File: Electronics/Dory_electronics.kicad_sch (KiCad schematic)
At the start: 10 parts, among them J1 Bateria 2s, J2 Conn_01x08, J3 Conn_01x08, J4 |Motor 2, J5 Motor 1, J6 sensor IR, U1 LM7805_TO220

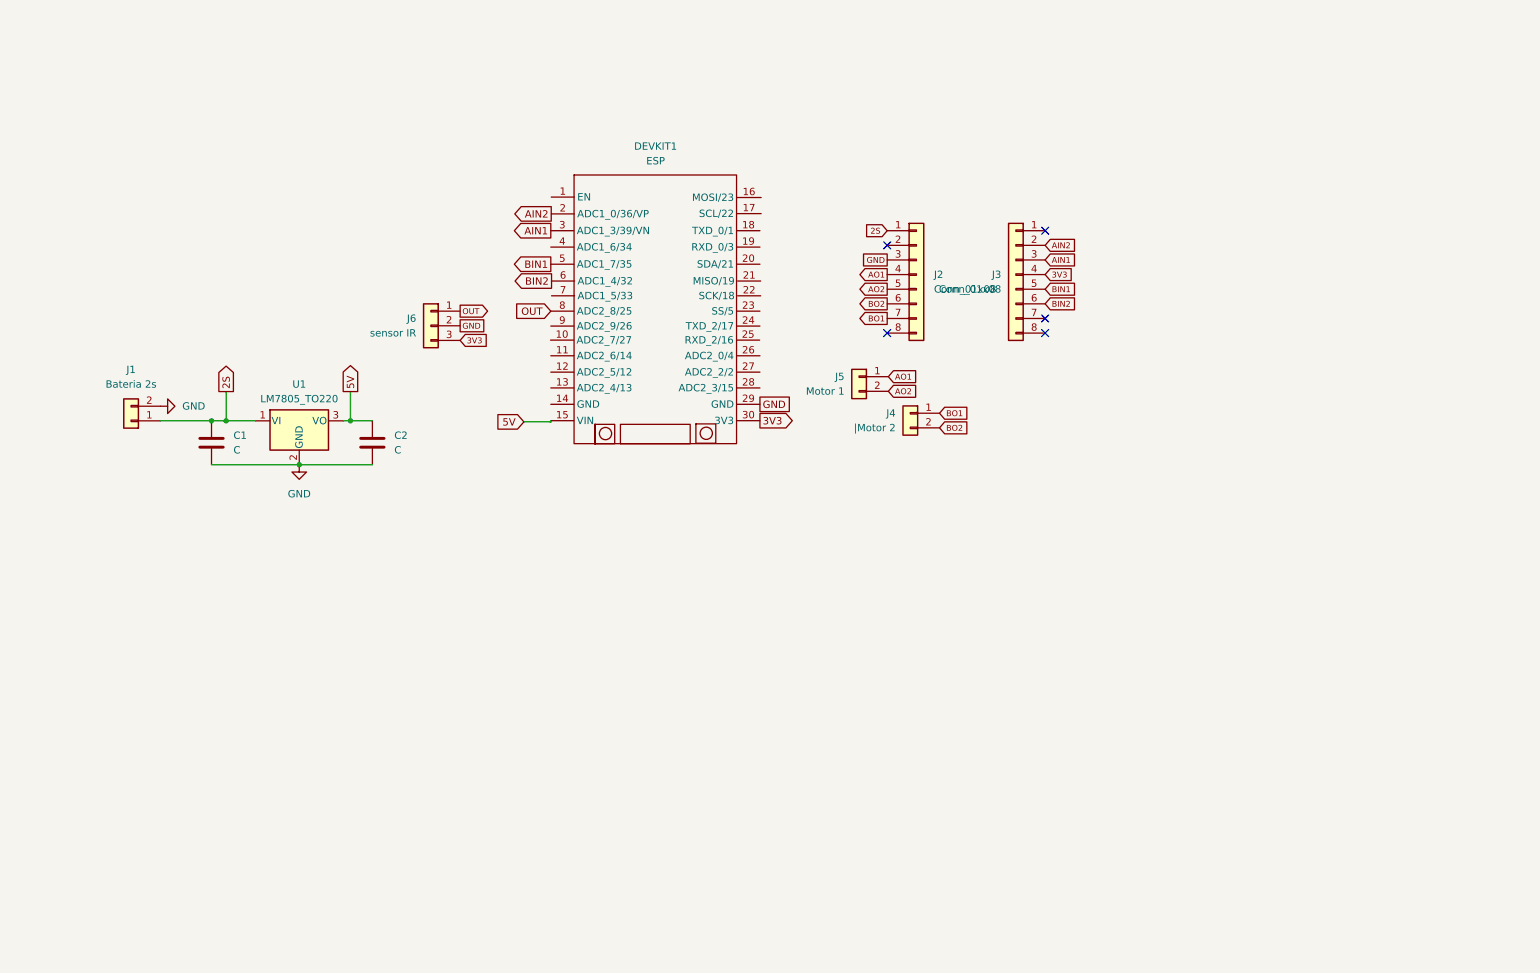
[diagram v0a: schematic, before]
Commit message: chore: organize schematic and add gitignore
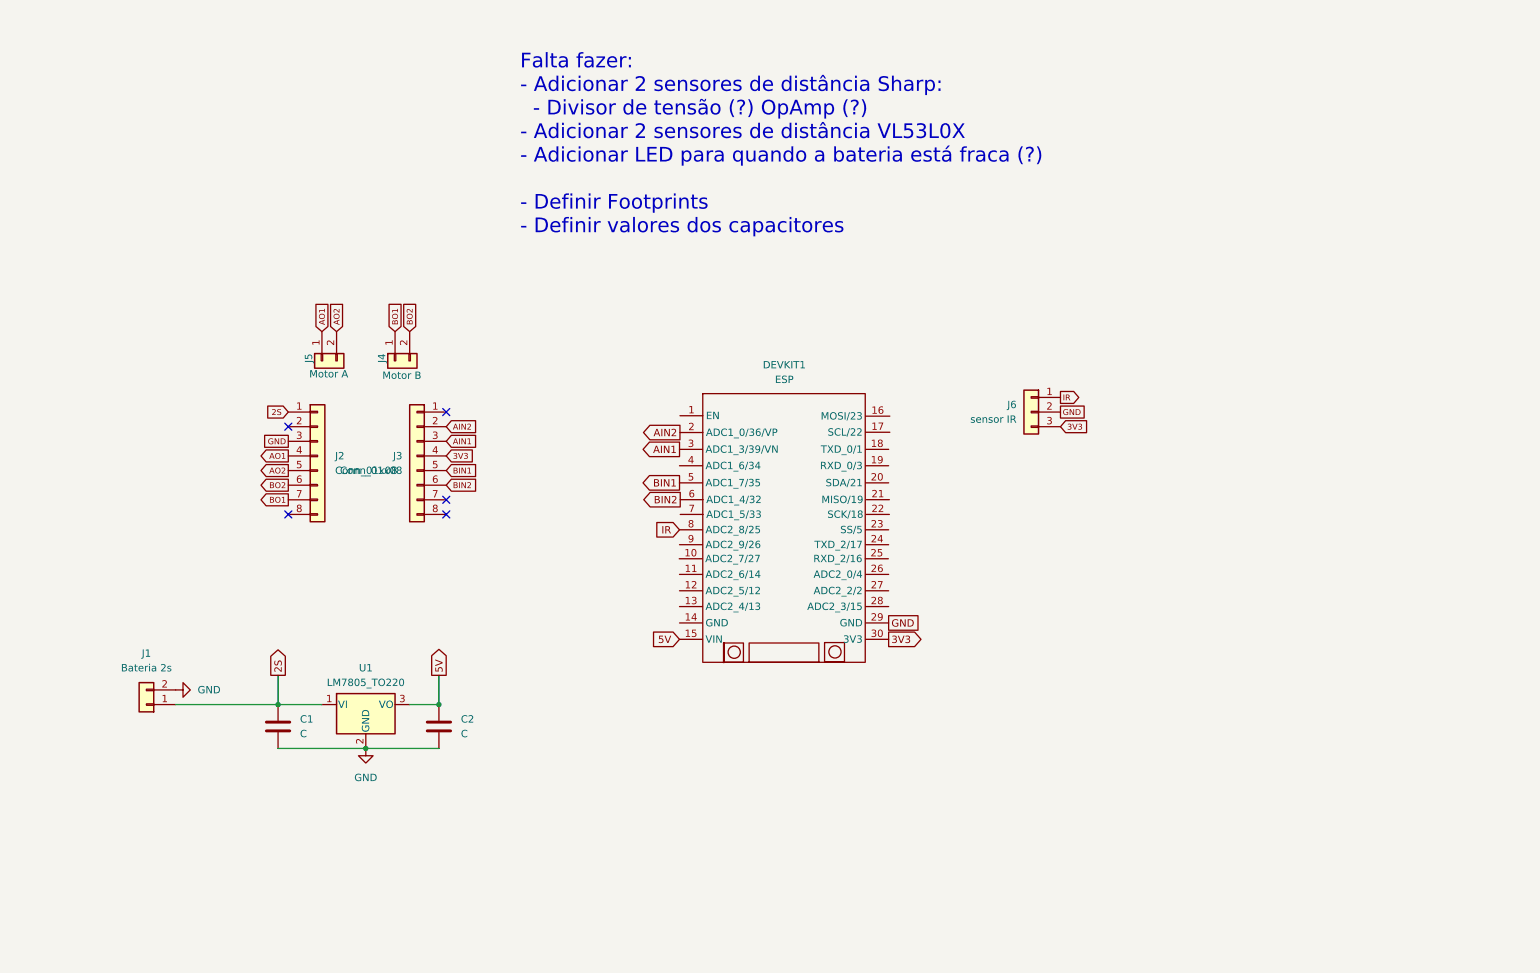
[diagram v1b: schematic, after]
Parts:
- J4: value |Motor 2 -> Motor B
- J5: value Motor 1 -> Motor A
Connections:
- net OUT renamed IR
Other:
- note added: "Falta fazer: - Adicionar 2 sensores de distância Sharp: - Divisor de tensão (?) OpAmp (?) - Adicionar 2 sensores de distância VL53L0X - Adicionar LED para quando a bateria está fraca (?) - Definir Footprints - Definir valores dos capacitores"
- moved on the sheet: C1, C2, DEVKIT1, J1, J2, J3, J4, J5, J6, U1

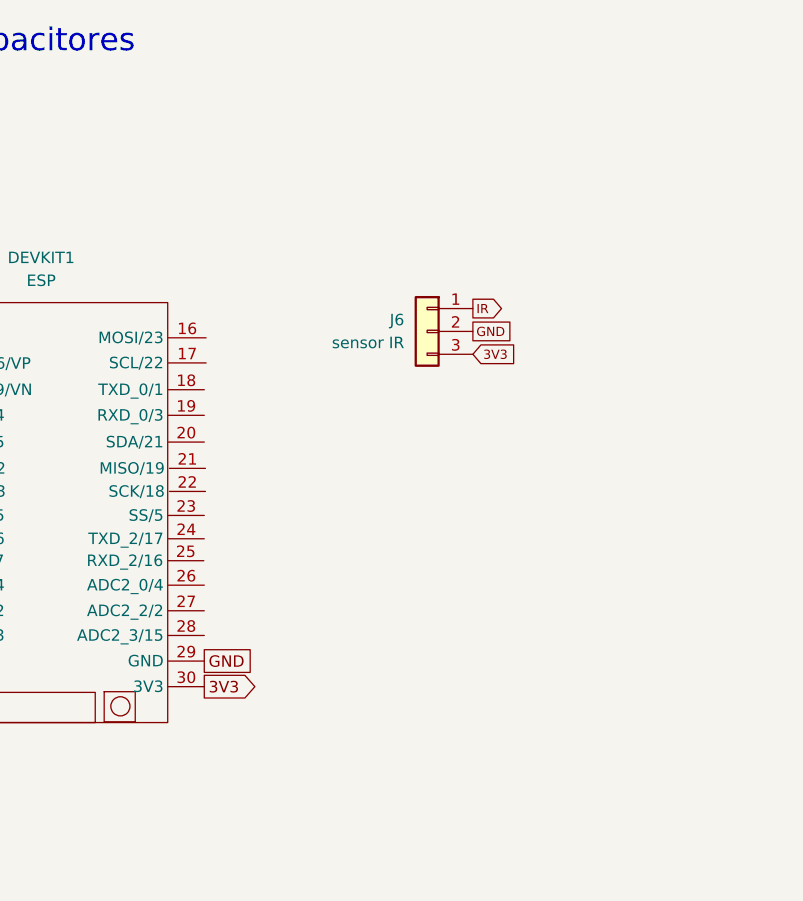
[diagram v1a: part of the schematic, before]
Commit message: feat: add VL530X
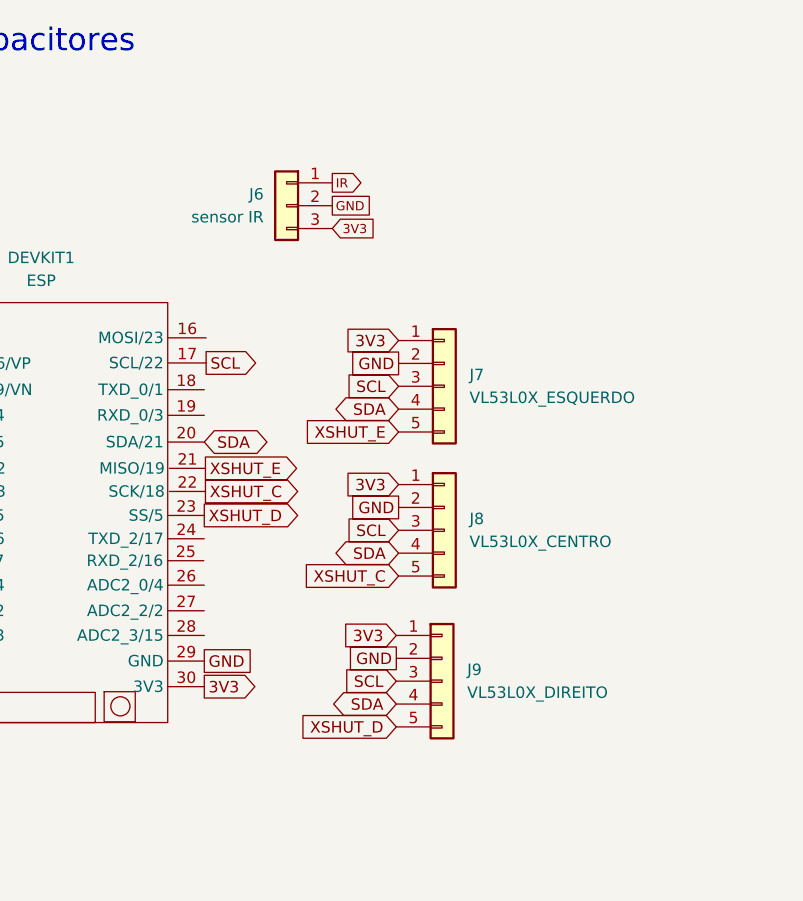
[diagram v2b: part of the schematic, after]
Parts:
- added J7: VL53L0X_ESQUERDO, symbol Connector_Generic:Conn_01x05
- added J8: VL53L0X_CENTRO, symbol Connector_Generic:Conn_01x05
- added J9: VL53L0X_DIREITO, symbol Connector_Generic:Conn_01x05
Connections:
- net 3V3: now also J7.1 (Pin_1), J8.1 (Pin_1), J9.1 (Pin_1)
- net GND: now also J7.2 (Pin_2), J8.2 (Pin_2), J9.2 (Pin_2)
- net SCL: now reaches DEVKIT1.17 (SCL/22)
- net SCL: now also J7.3 (Pin_3), J8.3 (Pin_3), J9.3 (Pin_3)
- net SDA: now reaches DEVKIT1.20 (SDA/21)
- net SDA: now also J7.4 (Pin_4), J8.4 (Pin_4), J9.4 (Pin_4)
- net XSHUT_E: now reaches DEVKIT1.21 (MISO/19)
- net XSHUT_E: now also J7.5 (Pin_5)
- net XSHUT_C: now reaches DEVKIT1.22 (SCK/18)
- net XSHUT_C: now also J8.5 (Pin_5)
- net XSHUT_D: now reaches DEVKIT1.23 (SS/5)
- net XSHUT_D: now also J9.5 (Pin_5)
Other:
- moved on the sheet: J6

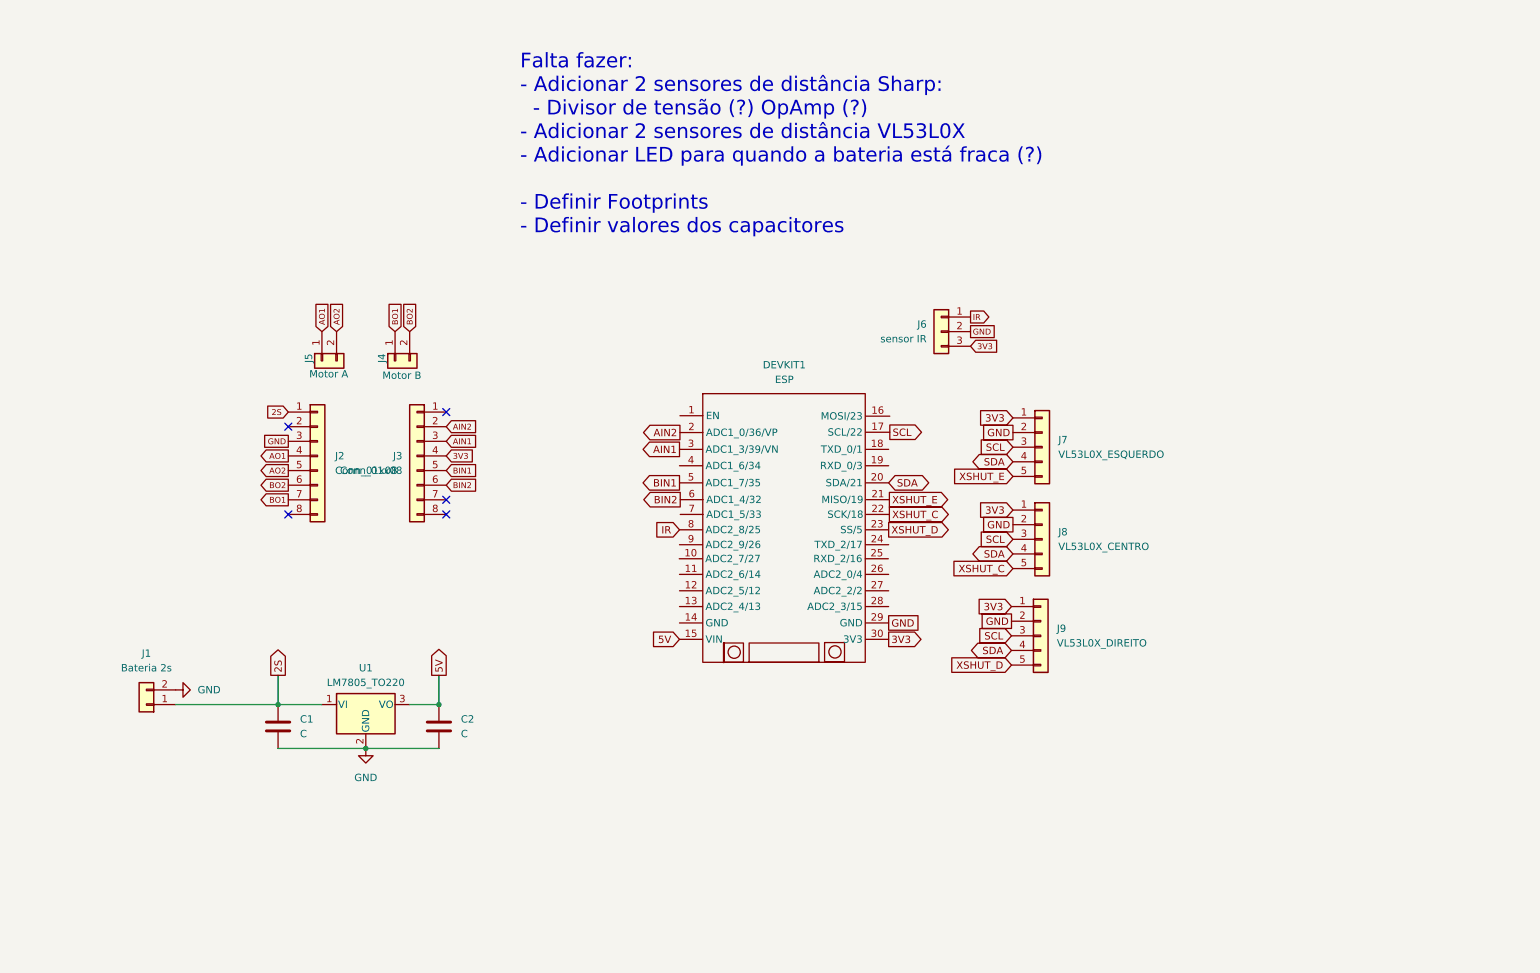
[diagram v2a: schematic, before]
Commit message: fix(Electronics): remove center vl53l0x from sch
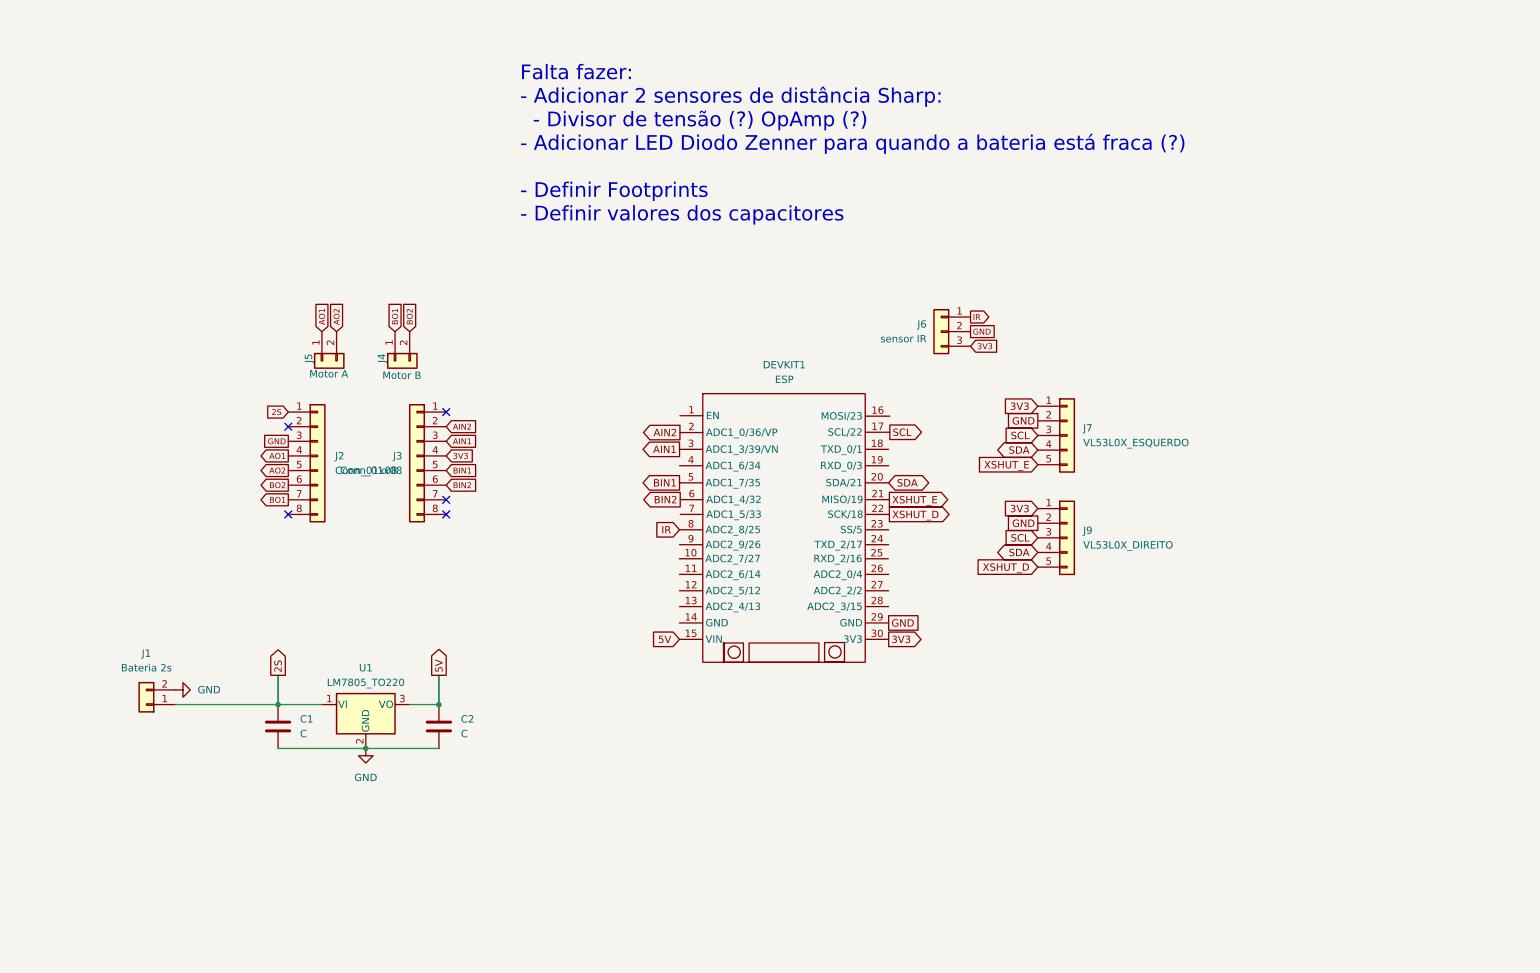
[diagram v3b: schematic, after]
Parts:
- removed J8: VL53L0X_CENTRO, symbol Connector_Generic:Conn_01x05
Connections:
- net XSHUT_C is gone; now on net XSHUT_D: DEVKIT1.22 (SCK/18)
- net XSHUT_D: no longer DEVKIT1.23 (SS/5)
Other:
- note added: "Falta fazer: - Adicionar 2 sensores de distância Sharp: - Divisor de tensão (?) OpAmp (?) - Adicionar LED Diodo Zenner para quando a bateria está fraca (?) - Definir Footprints - Definir valores dos capacitores"
- note removed: "Falta fazer: - Adicionar 2 sensores de distância Sharp: - Divisor de tensão (?) OpAmp (?) - Adicionar 2 sensores de distância VL53L0X - Adicionar LED para quando a bateria está fraca (?) - Definir Footprints - Definir valores dos capacitores"
- moved on the sheet: J7, J9

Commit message: chore: revision of the PCB
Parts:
- added J10: SHARP_CENTRO_E, symbol Connector_Generic:Conn_01x03
- added J8: SHARP_CENTRO_D, symbol Connector_Generic:Conn_01x03
- added R1, R2, R3, R4: R_Small_US, symbol Device:R_Small_US
- C1, C2: symbol Device:C -> Device:C_Polarized
- J1: value Bateria 2s -> Bateria 2S
- U1: value LM7805_TO220 -> LM1117 5V; footprint Package_TO_SOT_THT:TO-220-3_Vertical -> Package_TO_SOT_THT:TO-220-3_Horizontal_TabDown; symbol Regulator_Linear:LM7805_TO220 -> Regulator_Linear:LM1117T-5.0
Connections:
- net 2S: now also U1.3 (VI); no longer U1.1 (VI)
- net 5V: now also U1.2 (VO); no longer U1.3 (VO)
- net GND: now also U1.1 (GND), J10.2 (Pin_2), J8.2 (Pin_2), R2.2, R4.2; no longer U1.2 (GND)
- net ADC_CENTRO_D: now reaches DEVKIT1.27 (ADC2_2/2)
- net ADC_CENTRO_D: now also R1.2, R2.1
- net ADC_CENTRO_E: now reaches DEVKIT1.28 (ADC2_3/15)
- net ADC_CENTRO_E: now also R3.2, R4.1
- new net VCC: J10.3 (Pin_3), J8.3 (Pin_3)
- new net VO_CENTRO_D: J8.1 (Pin_1), R1.1
- new net VO_CENTRO_E: J10.1 (Pin_1), R3.1
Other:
- note added: "Falta fazer: - Mudar ADC_CENTRO_D de lugar (Pra n coincidir com o LED) - Adicionar LED Diodo Zenner para quando a bateria está fraca (?) - Definir Footprints - Definir valores dos capacitores e resistores - Colocar X nos pinos que não vamos usar Já fizemos: - Trocamos LM7805 pelo LM1117 - Mudamos pra capacitores eletrolíticos - Mudei a tag do sharp pra ter "CENTRO" no nome"
- note removed: "Falta fazer: - Adicionar 2 sensores de distância Sharp: - Divisor de tensão (?) OpAmp (?) - Adicionar LED Diodo Zenner para quando a bateria está fraca (?) - Definir Footprints - Definir valores dos capacitores"
- moved on the sheet: J1, J6, J7, J9, U1

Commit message: chore: update Electronics
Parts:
- added R6, R7: 4k7, symbol Device:R_Small_US
- C1: value C -> 10 uF
- C2: value C -> 100 uF
- R1, R3: value R_Small_US -> 7k5
- R2, R4: value R_Small_US -> 15k
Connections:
- net VCC is gone; now on net 5V: J10.3 (Pin_3), J8.3 (Pin_3)
- net 3V3: now also R6.2, R7.1
- net ADC_CENTRO_D: now also DEVKIT1.3 (ADC1_3/39/VN); no longer DEVKIT1.27 (ADC2_2/2)
- net ADC_CENTRO_E: now also DEVKIT1.2 (ADC1_0/36/VP); no longer DEVKIT1.28 (ADC2_3/15)
- net AIN1: now also DEVKIT1.4 (ADC1_6/34); no longer DEVKIT1.3 (ADC1_3/39/VN)
- net AIN2: now also DEVKIT1.5 (ADC1_7/35); no longer DEVKIT1.2 (ADC1_0/36/VP)
- net BIN1: now also DEVKIT1.6 (ADC1_4/32); no longer DEVKIT1.5 (ADC1_7/35)
- net BIN2: now also DEVKIT1.7 (ADC1_5/33); no longer DEVKIT1.6 (ADC1_4/32)
- net GND: now also DEVKIT1.14 (GND)
- net SCL: now also R6.1
- net SDA: now also R7.2
- no-connect marks 5 -> 20
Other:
- note added: "Falta fazer: - Adicionar LED Diodo Zenner para quando a bateria está fraca (?) - Definir Footprints Já fizemos: - Trocamos LM7805 pelo LM1117 - Mudamos pra capacitores eletrolíticos - Mudei a tag do sharp pra ter "CENTRO" no nome - Mudar ADC_CENTRO_D de lugar (Pra n coincidir com o LED) - Colocar X nos pinos que não vamos usar - Definir valores dos capacitores e resistores - Adicionar pull up I2C"
- note removed: "Falta fazer: - Mudar ADC_CENTRO_D de lugar (Pra n coincidir com o LED) - Adicionar LED Diodo Zenner para quando a bateria está fraca (?) - Definir Footprints - Definir valores dos capacitores e resistores - Colocar X nos pinos que não vamos usar Já fizemos: - Trocamos LM7805 pelo LM1117 - Mudamos pra capacitores eletrolíticos - Mudei a tag do sharp pra ter "CENTRO" no nome"
